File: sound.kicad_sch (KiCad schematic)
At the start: 18 parts, among them IC1 MAX4466EXK+T

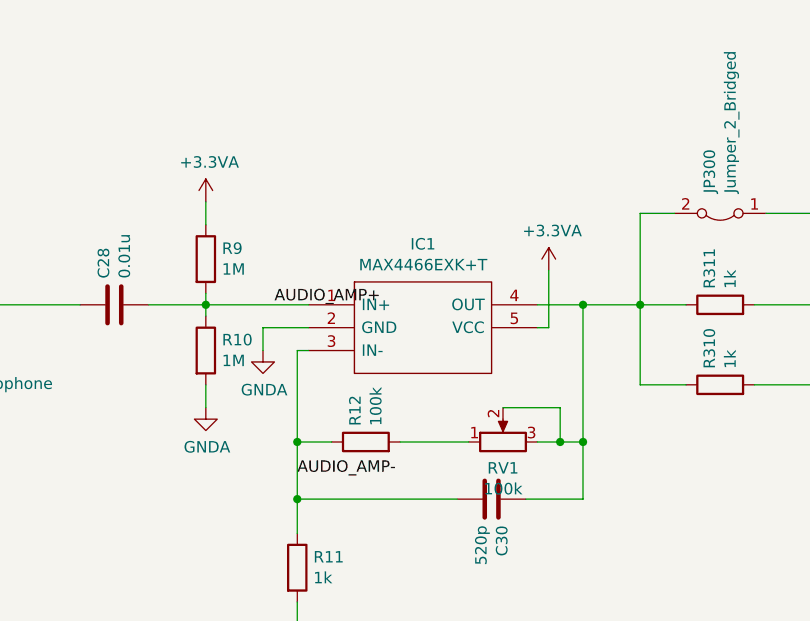
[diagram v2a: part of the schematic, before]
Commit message: Update to correct OP-amp. This is the version sent to production.
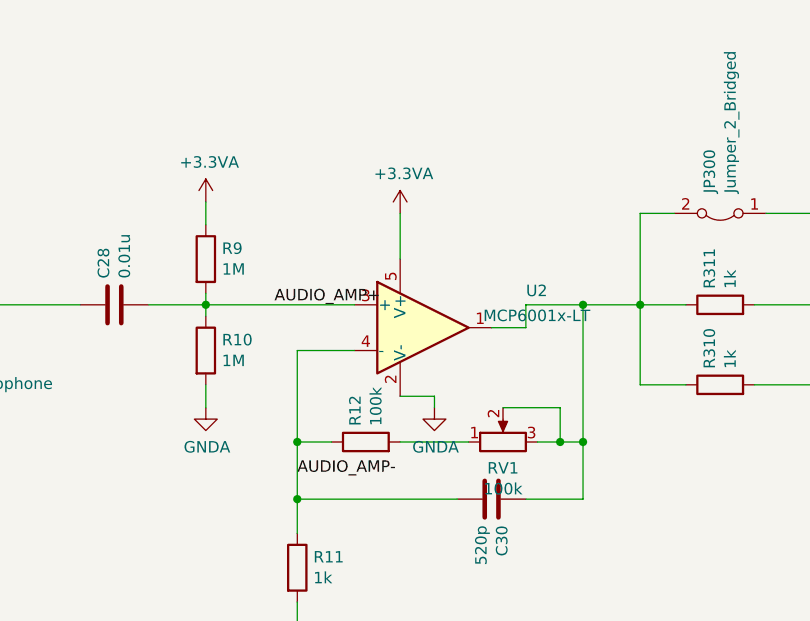
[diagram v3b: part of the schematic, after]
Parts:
- removed IC1: MAX4466EXK+T, Special_Parts:SOT65P210X110-5N, symbol Special_Parts:MAX4466EXK+T
- added U2: MCP6001x-LT, Package_TO_SOT_SMD:SOT-353_SC-70-5, symbol Amplifier_Operational:MCP6001x-LT
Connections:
- net +3.3VA: now also U2.5 (V+)
- net AUDIO_AMP+: now also U2.3 (+)
- net AUDIO_AMP-: now also U2.4 (-)
- net GNDA: now also U2.2 (V-)
- net at C30.1, JP300.2 (B), R310.1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: now also U2.1
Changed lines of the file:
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@@
+    (stroke (width 0) (type default) (color 0 0 0 0))
+  )
+  (wire (pts (xy 114.3 52.07) (xy 114.3 54.61))
     (stroke (width 0) (type default) (color 0 0 0 0))
   )
@@
     (stroke (width 0) (type default) (color 0 0 0 0))
   )
-  (wire (pts (xy 78.74 52.07) (xy 90.17 52.07))
+  (wire (pts (xy 78.74 52.07) (xy 95.25 52.07))
     (stroke (width 0) (type default) (color 0 0 0 0))
   )
@@
     (stroke (width 0) (type default) (color 0 0 0 0))
   )
-  (wire (pts (xy 120.65 52.07) (xy 115.57 52.07))
+  (wire (pts (xy 114.3 52.07) (xy 120.65 52.07))
     (stroke (width 0) (type default) (color 0 0 0 0))
   )
@@
     (stroke (width 0) (type default) (color 0 0 0 0))
   )
-  (wire (pts (xy 116.84 54.61) (xy 115.57 54.61))
-    (stroke (width 0) (type default) (color 0 0 0 0))
-  )
   (wire (pts (xy 88.9 67.31) (xy 88.9 73.66))
     (stroke (width 0) (type default) (color 0 0 0 0))
@@
     (stroke (width 0) (type default) (color 0 0 0 0))
   )
-  (wire (pts (xy 85.09 54.61) (xy 85.09 57.15))
-    (stroke (width 0) (type default) (color 0 0 0 0))
-  )
   (wire (pts (xy 78.74 50.8) (xy 78.74 52.07))
     (stroke (width 0) (type default) (color 0 0 0 0))
@@
     (stroke (width 0) (type default) (color 0 0 0 0))
   )
-  (wire (pts (xy 116.84 48.26) (xy 116.84 54.61))
-    (stroke (width 0) (type default) (color 0 0 0 0))
-  )
   (wire (pts (xy 33.02 36.83) (xy 41.91 36.83))
     (stroke (width 0) (type default) (color 0 0 0 0))
@@
     (stroke (width 0) (type default) (color 0 0 0 0))
   )
-  (wire (pts (xy 90.17 54.61) (xy 85.09 54.61))
-    (stroke (width 0) (type default) (color 0 0 0 0))
-  )
   (wire (pts (xy 118.11 67.31) (xy 120.65 67.31))
     (stroke (width 0) (type default) (color 0 0 0 0))
@@
     (stroke (width 0) (type default) (color 0 0 0 0))
   )
+  (wire (pts (xy 104.14 62.23) (xy 100.33 62.23))
+    (stroke (width 0) (type default) (color 0 0 0 0))
+  )
   (wire (pts (xy 160.02 67.31) (xy 165.1 67.31))
     (stroke (width 0) (type default) (color 0 0 0 0))
@@
     (stroke (width 0) (type default) (color 0 0 0 0))
   )
+  (wire (pts (xy 114.3 54.61) (xy 110.49 54.61))
+    (stroke (width 0) (type default) (color 0 0 0 0))
+  )
   (wire (pts (xy 120.65 52.07) (xy 127 52.07))
     (stroke (width 0) (type default) (color 0 0 0 0))
@@
     (stroke (width 0) (type default) (color 0 0 0 0))
   )
+  (wire (pts (xy 100.33 41.91) (xy 100.33 46.99))
+    (stroke (width 0) (type default) (color 0 0 0 0))
+  )
   (wire (pts (xy 170.18 55.88) (xy 170.18 52.07))
     (stroke (width 0) (type default) (color 0 0 0 0))
@@
     (stroke (width 0) (type default) (color 0 0 0 0))
   )
-  (wire (pts (xy 88.9 57.15) (xy 90.17 57.15))
+  (wire (pts (xy 88.9 57.15) (xy 95.25 57.15))
     (stroke (width 0) (type default) (color 0 0 0 0))
   )
@@
   )
   (wire (pts (xy 41.91 39.37) (xy 48.26 39.37))
+    (stroke (width 0) (type default) (color 0 0 0 0))
+  )
+  (wire (pts (xy 104.14 62.23) (xy 104.14 63.5))
     (stroke (width 0) (type default) (color 0 0 0 0))
   )
@@
     )
   )
-  (symbol (lib_id "Special_Parts:MAX4466EXK+T") (at 90.17 52.07 0) (unit 1)
-    (in_bom yes) (on_board yes)
-    (property "Reference" "IC1" (id 0) (at 102.87 45.339 0))
-    (property "Value" "MAX4466EXK+T" (id 1) (at 102.87 47.6504 0))
-    (property "Footprint" "Special_Parts:SOT65P210X110-5N" (id 2) (at 111.76 49.53 0)
-      (effects (font (size 1.27 1.27)) (justify left) hide)
-    )
-    (property "Datasheet" "https://datasheets.maximintegrated.com/en/ds/MAX4465-MAX4469.pdf" (id 3) (at 111.76 52.07 0)
-      (effects (font (size 1.27 1.27)) (justify left) hide)
-    )
-    (property "Description" "Microphone Preamplifiers uPower Microphone Preamplifier" (id 4) (at 111.76 54.61 0)
-      (effects (font (size 1.27 1.27)) (justify left) hide)
-    )
-    (property "Height" "1.1" (id 5) (at 111.76 57.15 0)
-      (effects (font (size 1.27 1.27)) (justify left) hide)
-    )
-    (property "Mouser Part Number" "700-MAX4466EXKT" (id 6) (at 111.76 59.69 0)
-      (effects (font (size 1.27 1.27)) (justify left) hide)
-    )
-    (property "Mouser Price/Stock" "https://www.mouser.co.uk/ProductDetail/Maxim-Integrated/MAX4466EXK%2bT?qs=1eQvB6Dk1viIfH6l6v5sWg%3D%3D" (id 7) (at 111.76 62.23 0)
-      (effects (font (size 1.27 1.27)) (justify left) hide)
-    )
-    (property "Manufacturer_Name" "Maxim Integrated" (id 8) (at 111.76 64.77 0)
-      (effects (font (size 1.27 1.27)) (justify left) hide)
-    )
-    (property "Manufacturer_Part_Number" "MAX4466EXK+T" (id 9) (at 111.76 67.31 0)
-      (effects (font (size 1.27 1.27)) (justify left) hide)
-    )
-    (pin "1")
-    (pin "2")
-    (pin "3")
-    (pin "4")
-    (pin "5")
-  )
-  (symbol (lib_id "power:GNDA") (at 85.09 57.15 0) (unit 1)
-    (in_bom yes) (on_board yes)
-    (property "Reference" "#PWR0106" (id 0) (at 85.09 63.5 0)
-      (effects (font (size 1.27 1.27)) hide)
-    )
-    (property "Value" "GNDA" (id 1) (at 85.217 61.5442 0))
-    (property "Footprint" "" (id 2) (at 85.09 57.15 0)
-      (effects (font (size 1.27 1.27)) hide)
-    )
-    (property "Datasheet" "" (id 3) (at 85.09 57.15 0)
-      (effects (font (size 1.27 1.27)) hide)
-    )
-    (pin "1")
-  )
-  (symbol (lib_id "power:+3.3VA") (at 116.84 48.26 0) (unit 1)
-    (in_bom yes) (on_board yes)
-    (property "Reference" "#PWR0107" (id 0) (at 116.84 52.07 0)
-      (effects (font (size 1.27 1.27)) hide)
-    )
-    (property "Value" "+3.3VA" (id 1) (at 117.221 43.8658 0))
-    (property "Footprint" "" (id 2) (at 116.84 48.26 0)
-      (effects (font (size 1.27 1.27)) hide)
-    )
-    (property "Datasheet" "" (id 3) (at 116.84 48.26 0)
+  (symbol (lib_id "power:GNDA") (at 104.14 63.5 0) (unit 1)
+    (in_bom yes) (on_board yes)
+    (property "Reference" "#PWR0106" (id 0) (at 104.14 69.85 0)
+      (effects (font (size 1.27 1.27)) hide)
+    )
+    (property "Value" "GNDA" (id 1) (at 104.267 67.8942 0))
+    (property "Footprint" "" (id 2) (at 104.14 63.5 0)
+      (effects (font (size 1.27 1.27)) hide)
+    )
+    (property "Datasheet" "" (id 3) (at 104.14 63.5 0)
+      (effects (font (size 1.27 1.27)) hide)
+    )
+    (pin "1")
+  )
+  (symbol (lib_id "power:+3.3VA") (at 100.33 41.91 0) (unit 1)
+    (in_bom yes) (on_board yes)
+    (property "Reference" "#PWR0107" (id 0) (at 100.33 45.72 0)
+      (effects (font (size 1.27 1.27)) hide)
+    )
+    (property "Value" "+3.3VA" (id 1) (at 100.711 37.5158 0))
+    (property "Footprint" "" (id 2) (at 100.33 41.91 0)
+      (effects (font (size 1.27 1.27)) hide)
+    )
+    (property "Datasheet" "" (id 3) (at 100.33 41.91 0)
       (effects (font (size 1.27 1.27)) hide)
     )
@@
     (pin "1")
   )
+  (symbol (lib_id "Amplifier_Operational:MCP6001x-LT") (at 102.87 54.61 0) (unit 1)
+    (in_bom yes) (on_board yes) (fields_autoplaced)
+    (property "Reference" "U2" (id 0) (at 115.5042 50.5165 0))
+    (property "Value" "MCP6001x-LT" (id 1) (at 115.5042 53.2916 0))
+    (property "Footprint" "Package_TO_SOT_SMD:SOT-353_SC-70-5" (id 2) (at 100.33 59.69 0)
+      (effects (font (size 1.27 1.27)) (justify left) hide)
+    )
+    (property "Datasheet" "http://ww1.microchip.com/downloads/en/DeviceDoc/21733j.pdf" (id 3) (at 102.87 54.61 0)
+      (effects (font (size 1.27 1.27)) hide)
+    )
+    (pin "2")
+    (pin "5")
+    (pin "1")
+    (pin "3")
+    (pin "4")
+  )
 )

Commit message: Fixed known errors. * Reset curcuit, know is pull high with button tieing it low * OP-amp now uses correct, larger, footprint.
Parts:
- U2: footprint Package_TO_SOT_SMD:SOT-353_SC-70-5 -> Package_TO_SOT_SMD:SOT-23-5
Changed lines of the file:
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@@
     (property "Reference" "U2" (id 0) (at 115.5042 50.5165 0))
     (property "Value" "MCP6001x-LT" (id 1) (at 115.5042 53.2916 0))
-    (property "Footprint" "Package_TO_SOT_SMD:SOT-353_SC-70-5" (id 2) (at 100.33 59.69 0)
+    (property "Footprint" "Package_TO_SOT_SMD:SOT-23-5" (id 2) (at 100.33 59.69 0)
       (effects (font (size 1.27 1.27)) (justify left) hide)
     )
